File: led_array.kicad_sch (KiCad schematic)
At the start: 3 parts, among them U5 74AHCT1G125

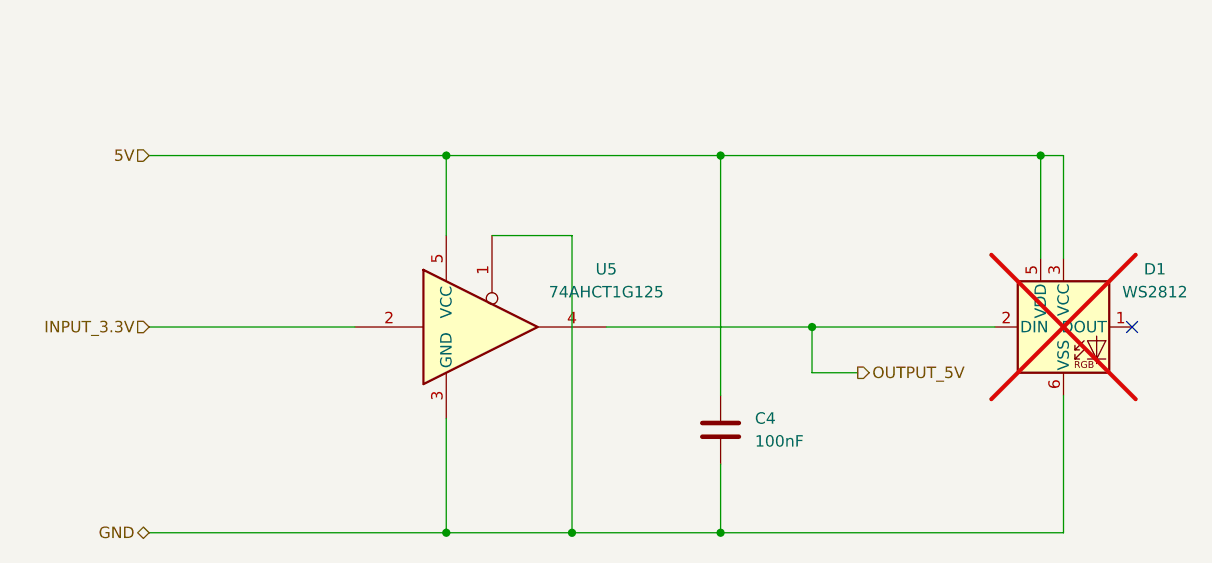
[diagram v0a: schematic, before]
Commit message: Re-labelled all parts.
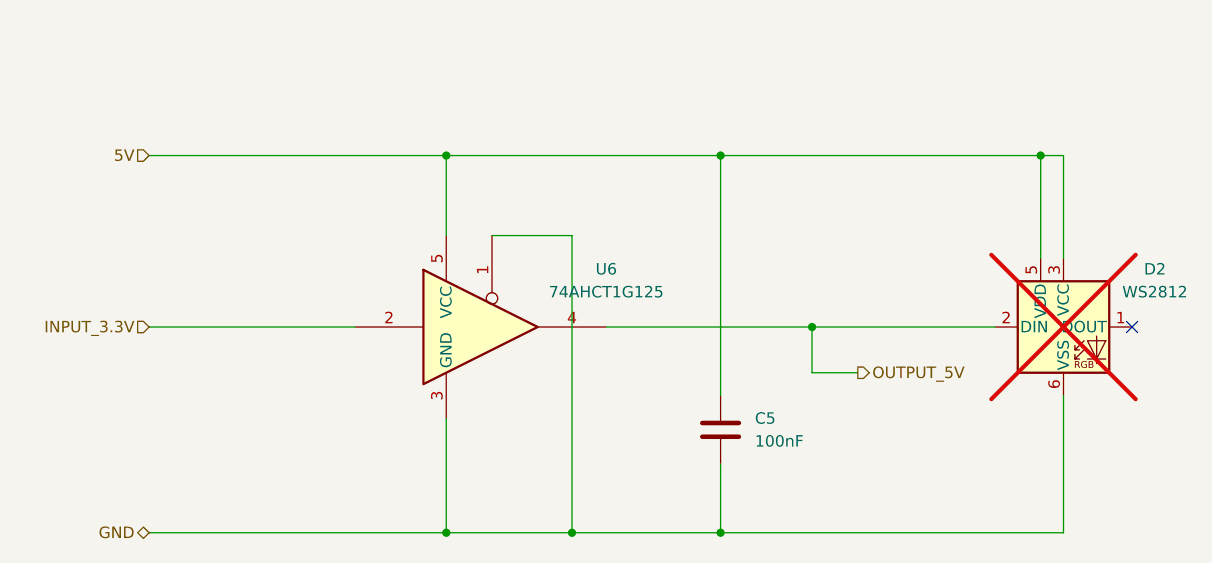
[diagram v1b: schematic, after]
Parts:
- renumbered C4 to C5, D1 to D2, U5 to U6
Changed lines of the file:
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@@
 		(dnp yes)
 		(fields_autoplaced yes)
-		(property "Reference" "D1"
+		(property "Reference" "D2"
 			(at 170.18 41.8398 0)
 			(effects
@@
 			(project "universal-board"
 				(path "/64404f27-cfd6-41d9-8edb-810ebab8cc14/b28a21dd-1aff-4e24-a93f-dbc2ef34d4d1"
-					(reference "D1")
+					(reference "D2")
 					(unit 1)
 				)
@@
 		(dnp no)
 		(fields_autoplaced yes)
-		(property "Reference" "C4"
+		(property "Reference" "C5"
 			(at 125.73 58.4199 0)
 			(effects
@@
 			(project ""
 				(path "/64404f27-cfd6-41d9-8edb-810ebab8cc14/b28a21dd-1aff-4e24-a93f-dbc2ef34d4d1"
-					(reference "C4")
+					(reference "C5")
 					(unit 1)
 				)
@@
 		(dnp no)
 		(fields_autoplaced yes)
-		(property "Reference" "U5"
+		(property "Reference" "U6"
 			(at 109.22 41.8398 0)
 			(effects
@@
 			(project "universal-board"
 				(path "/64404f27-cfd6-41d9-8edb-810ebab8cc14/b28a21dd-1aff-4e24-a93f-dbc2ef34d4d1"
-					(reference "U5")
+					(reference "U6")
 					(unit 1)
 				)

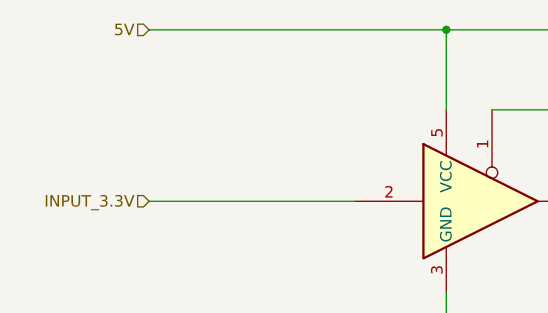
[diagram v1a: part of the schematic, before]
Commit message: ERC fixes.
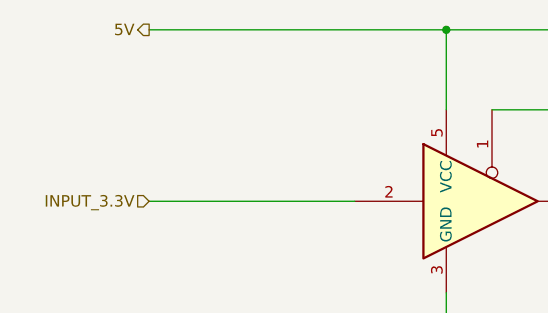
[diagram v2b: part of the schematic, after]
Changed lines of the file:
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@@
 	)
 	(hierarchical_label "5V"
-		(shape input)
+		(shape output)
 		(at 58.42 29.21 180)
 		(effects

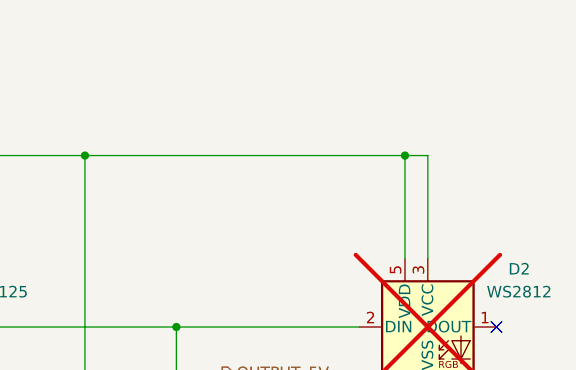
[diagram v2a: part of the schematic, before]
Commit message: Moved some components around for better readability.
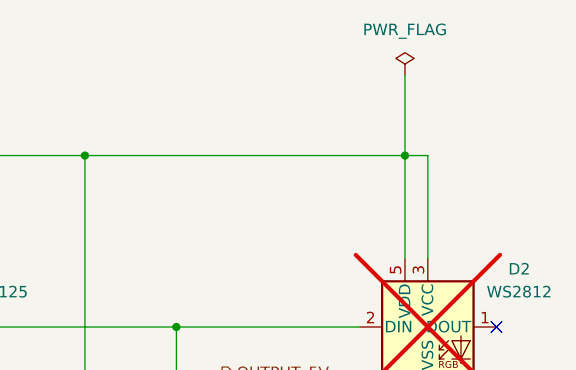
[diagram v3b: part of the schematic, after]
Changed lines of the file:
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@@
+	(wire
+		(pts
+			(xy 157.48 20.32) (xy 157.48 29.21)
+		)
+		(stroke
+			(width 0)
+			(type default)
+		)
+	)
 	(wire
 		(pts
@@
 					(unit 1)
 				)
+			)
+		)
+	)
+	(symbol
+		(lib_id "power:PWR_FLAG")
+		(at 157.48 20.32 0)
+		(unit 1)
+		(exclude_from_sim no)
+		(in_bom yes)
+		(on_board yes)
+		(dnp no)
+		(fields_autoplaced yes)
+		(property "Reference" "#FLG01"
+			(at 157.48 18.415 0)
+			(effects
+				(font
+					(size 1.27 1.27)
+				)
+				(hide yes)
+			)
+		)
+		(property "Value" "PWR_FLAG"
+			(at 157.48 15.24 0)
+			(effects
+				(font
+					(size 1.27 1.27)
+				)
+			)
+		)
+		(property "Footprint" ""
+			(at 157.48 20.32 0)
+			(effects
+				(font
+					(size 1.27 1.27)
+				)
+				(hide yes)
+			)
+		)
+		(property "Datasheet" "~"
+			(at 157.48 20.32 0)
+			(effects
+				(font
+					(size 1.27 1.27)
+				)
+				(hide yes)
+			)
+		)
+		(property "Description" "Special symbol for telling ERC where power comes from"
+			(at 157.48 20.32 0)
+			(effects
+				(font
+					(size 1.27 1.27)
+				)
+				(hide yes)
+			)
+		)
+		(pin "1"
+		)
+		(instances
+			(project ""
+				(path "/64404f27-cfd6-41d9-8edb-810ebab8cc14/b28a21dd-1aff-4e24-a93f-dbc2ef34d4d1"
+					(reference "#FLG01")
+					(unit 1)
+				)

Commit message: Reorganized board to be on one sheet.
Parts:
- removed C5: 100nF, symbol Device:C
- removed D2: WS2812, LED_SMD:LED_WS2812_PLCC6_5.0x5.0mm_P1.6mm, symbol LED:WS2812
- removed U6: 74AHCT1G125, symbol 74xGxx:74AHCT1G125
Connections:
- no-connect marks 1 -> 0
